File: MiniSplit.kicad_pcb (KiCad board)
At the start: 2 copper layers, 135 x 80 mm, 49 parts, among them J1 5PIN, SW1 SW_PUSH, SW10 SW_PUSH, SW11 SW_PUSH, SW12 SW_PUSH, SW13 SW_PUSH, SW14 SW_PUSH, SW15 SW_PUSH, SW16 SW_PUSH, SW17 SW_PUSH, SW18 SW_PUSH, SW19 SW_PUSH, SW2 SW_PUSH, SW20 SW_PUSH, SW21 SW_PUSH, SW3 SW_PUSH, SW4 SW_PUSH, SW5 SW_PUSH, SW6 SW_PUSH, SW7 SW_PUSH, SW8 SW_PUSH, SW9 SW_PUSH, U1 HOLE, U1 ProMicro, U2 HOLE, U3 HOLE, U4 HOLE

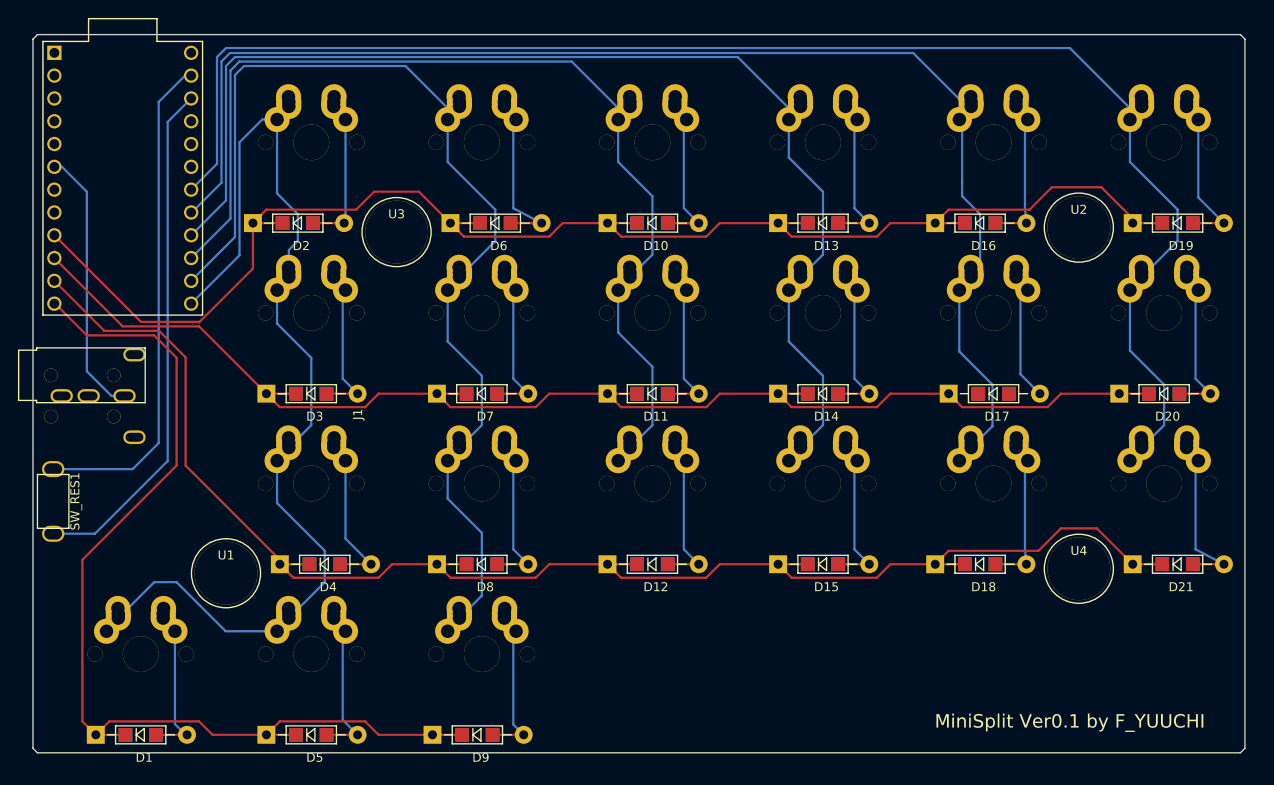
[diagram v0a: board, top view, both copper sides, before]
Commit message: ✨ver0.1→0.2✨
fix:Switch Hole,TRRS Jack Silk
add:icon
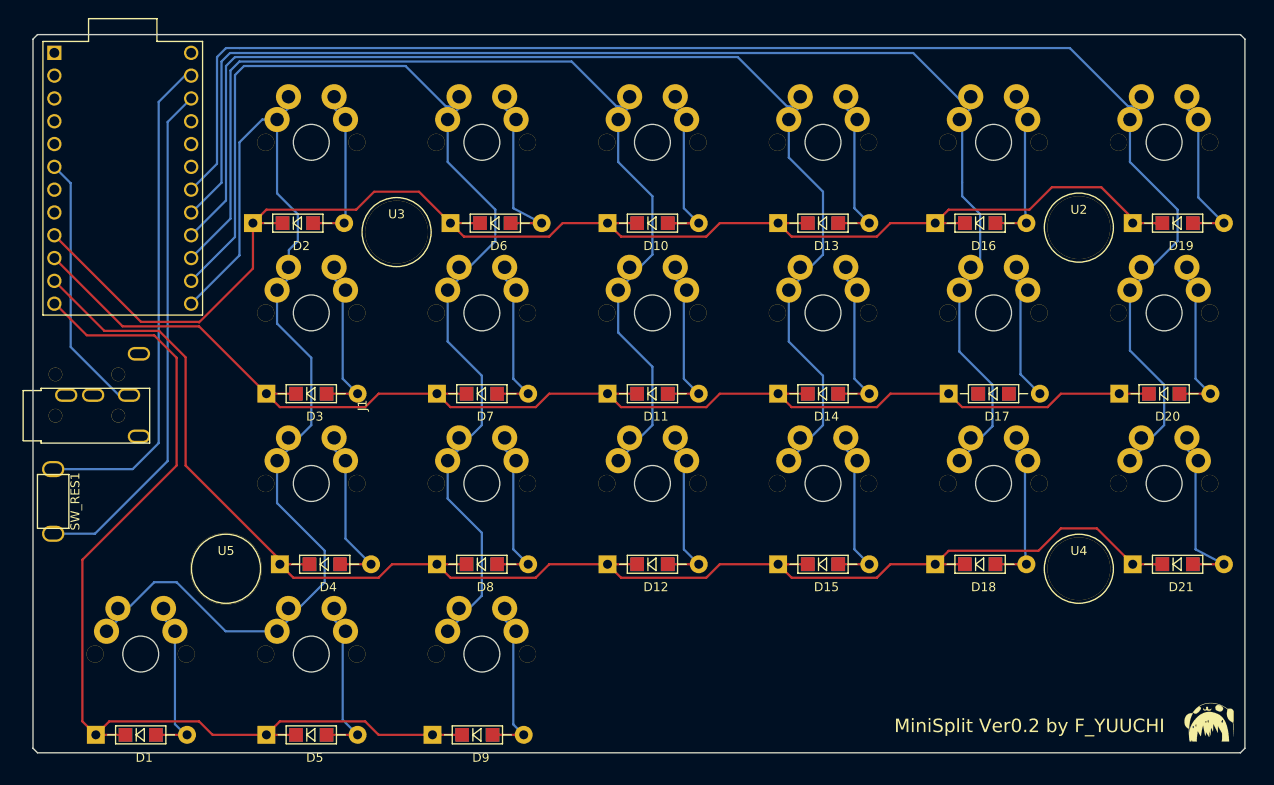
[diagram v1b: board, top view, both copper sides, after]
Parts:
- removed the U1 at (121.5, 110.0)
- added G***: LOGO, minisplit-footprint:icon_logo, F.Cu at (231.0, 126.0)
- added U5: HOLE, library:hole, F.Cu at (121.5, 109.5)
- SW1, SW10, SW11, SW12, SW13, SW14, SW15, SW16, SW17, SW18, SW19, SW2, SW20, SW21, SW3, SW4, SW5, SW6, SW7, SW8, SW9: footprint lets_split-footprint:MXALPS_FLIP_HOLES -> minisplit-footprint:MX_FLIP_HOLES
- moved J1 1.12 mm to (113.0, 90.0)
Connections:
- J1 pad 1: VCC -> (no net)
- J1 pad 2: Net-(J1-Pad2) -> (no net)
- U1 pad 1: Net-(U1-Pad1) -> (no net)
- U1 pad 19: Net-(U1-Pad19) -> (no net)
- U1 pad 2: Net-(U1-Pad2) -> (no net)
- U1 pad 20: Net-(U1-Pad20) -> (no net)
- U1 pad 21: Net-(U1-Pad21) -> (no net)
- U1 pad 24: Net-(U1-Pad24) -> (no net)
- U1 pad 3: Net-(U1-Pad3) -> (no net)
- U1 pad 4: Net-(U1-Pad4) -> (no net)
- U1 pad 5: Net-(U1-Pad5) -> (no net)
- U1 pad 7: Net-(U1-Pad7) -> (no net)
- U1 pad 8: Net-(U1-Pad8) -> (no net)
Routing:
- net col4: track 147.3 -> 151.3 mm
- net sda: track 30.1 -> 29.5 mm
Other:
- board text added: "MiniSplit Ver0.2 by F_YUUCHI"
- board text removed: "MiniSplit Ver0.1 by F_YUUCHI"

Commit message: SizeCange
130mm×85mm→127mm×83.5mm
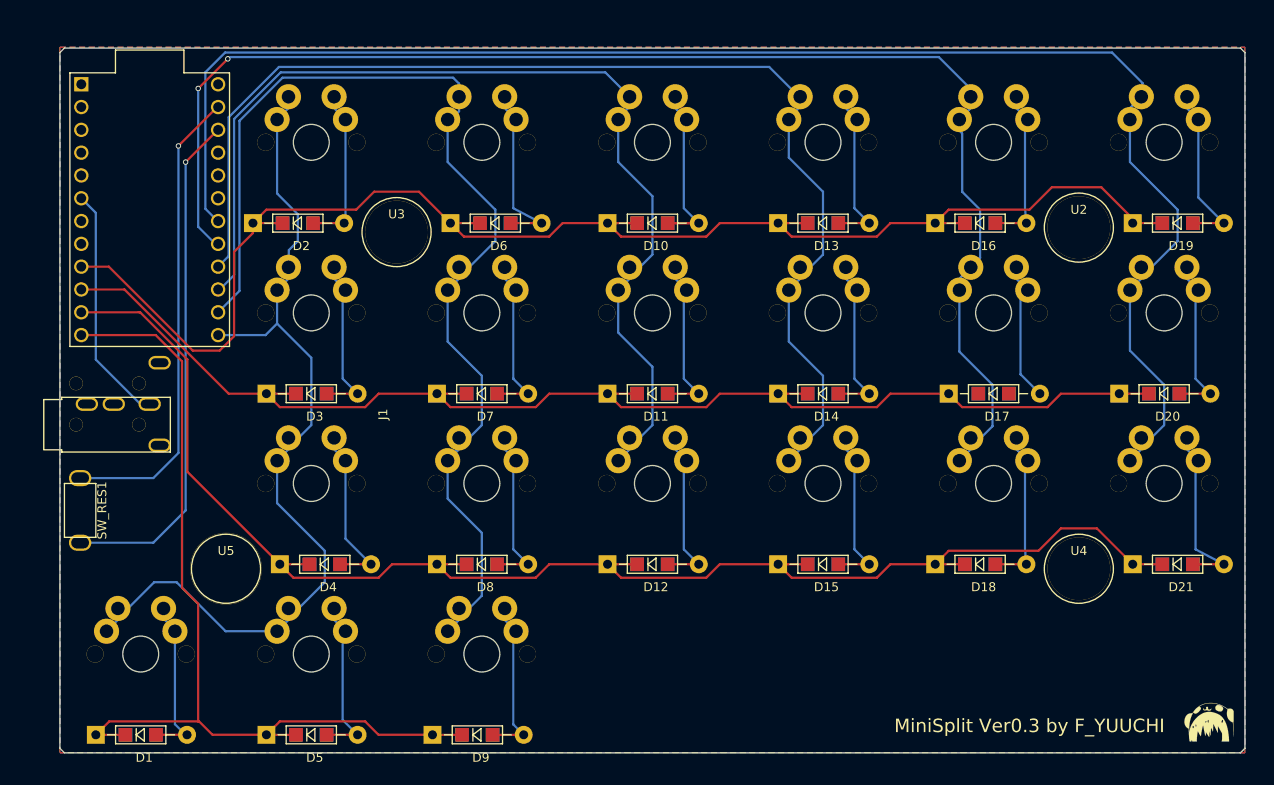
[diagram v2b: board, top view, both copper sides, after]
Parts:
- moved U1 4.61 mm to (113.0, 69.5)
- moved SW_RES1 3.16 mm to (107.0, 103.0)
- moved J1 2.51 mm to (115.3, 91.0)
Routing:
- net col0: track 117.5 -> 99.2 mm
- net row3: track 113.0 -> 103.2 mm
- net col4: track 151.3 -> 156.2 mm, vias 0 -> 2
- net row1: track 147.6 -> 143.2 mm
- net col5: track 169.8 -> 174.1 mm
- net row2: track 168.6 -> 164.7 mm
- net GND: track 55.8 -> 52.5 mm, vias 0 -> 1
- net sda: track 29.5 -> 26.7 mm
- net col2: track 116.0 -> 113.5 mm
- net col3: track 133.5 -> 132.1 mm
- net row0: track 162.2 -> 163.6 mm
- net Net-(SW_RES1-Pad1): track 57.6 -> 57.1 mm, vias 0 -> 1
- added copper zone on B.Cu, net GND
- added copper zone on F.Cu, net GND
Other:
- board size 135 x 80 mm -> 132 x 78.5 mm
- board text added: "MiniSplit Ver0.3 by F_YUUCHI"
- board text removed: "MiniSplit Ver0.2 by F_YUUCHI"

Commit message: ✨ver0.2→1.0✨
42keys→50keys
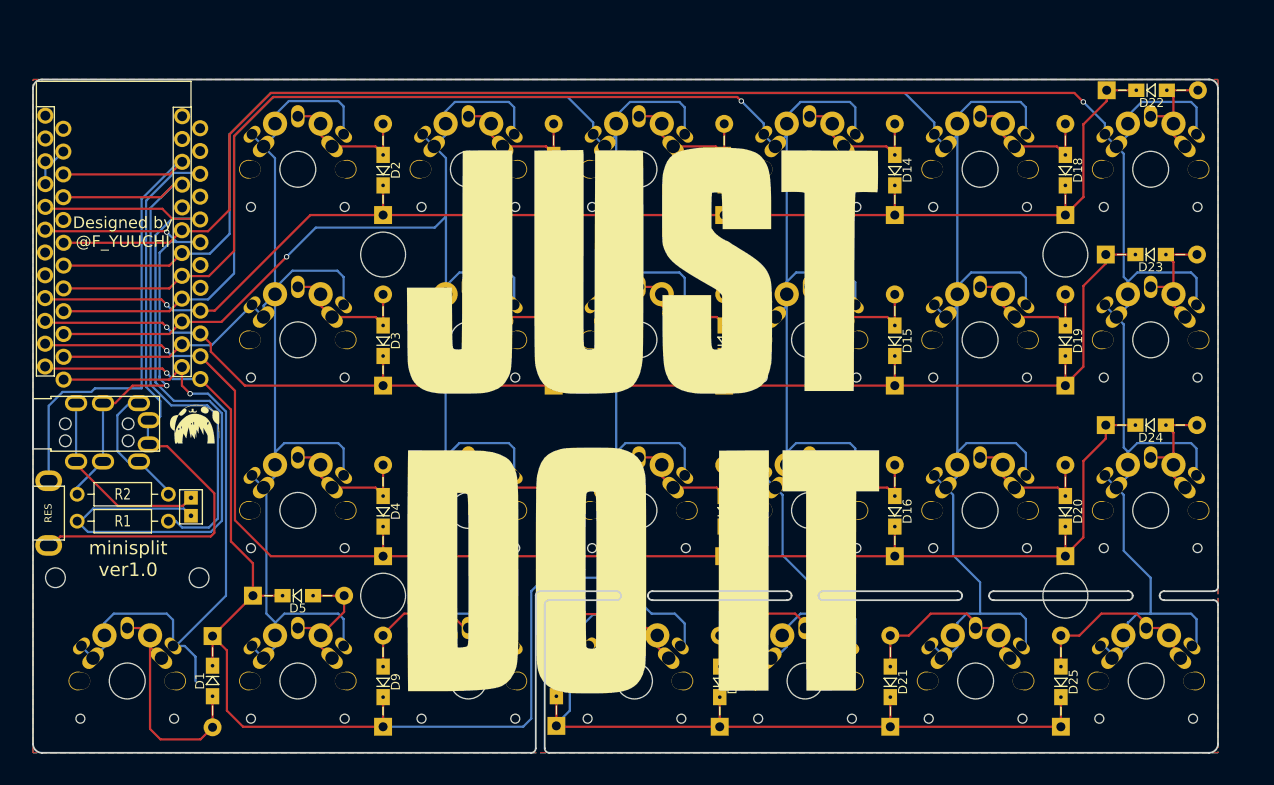
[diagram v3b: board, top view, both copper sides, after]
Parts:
- removed the G*** at (231.0, 126.0)
- removed SW1, SW10, SW11, SW12, SW13, SW14, SW15, SW16, SW17, SW18, SW19, SW2, SW20, SW21, SW3, SW4, SW5, SW6, SW7, SW8, SW9: SW_PUSH, minisplit-footprint:MX_FLIP_HOLES
- removed SW_RES1: SW_PUSH, minisplit-footprint:TACT_SWITCH_TVBP06
- removed the U1 at (113.0, 69.5)
- removed U2, U3, U4, U5: HOLE, library:hole
- added D22: D, minisplit2-footprint:Diode_TH_SOD123, F.Cu at (224.6, 56.2)
- added D23: D, minisplit2-footprint:Diode_TH_SOD123, F.Cu at (224.5, 74.5)
- added D24: D, minisplit2-footprint:Diode_TH_SOD123, F.Cu at (224.5, 93.5)
- added D25: D, minisplit2-footprint:Diode_TH_SOD123, F.Cu at (214.5, 122.1)
- added G***: LOGO, minisplit2-footprint:JUST_DO_IT, F.Cu at (168.0, 93.0)
- added G***: LOGO, minisplit2-footprint:icon_logo, F.Cu at (118.0, 92.8)
- added R1: R1, promicro:RESISTOR, F.Cu at (110.0, 104.2)
- added R2: R2, promicro:RESISTOR, F.Cu at (110.0, 101.2)
- added REF**: M2_HOLE, minisplit2-footprint:M2_HOLE, F.Cu at (102.5, 110.5)
- added REF**: M2_HOLE, minisplit2-footprint:M2_HOLE, F.Cu at (118.5, 110.5)
- added RES1: SW_PUSH, minisplit-footprint:TACT_SWITCH_TVBP06, F.Cu at (100.0, 103.3)
- added SW_1: SW_PUSH, minisplit2-footprint:MX_PG1350_FLIP_HOLES, F.Cu at (129.5, 65.0)
- added SW_11: SW_PUSH, minisplit2-footprint:MX_PG1350_FLIP_HOLES, F.Cu at (129.5, 84.0)
- added SW_12: SW_PUSH, minisplit2-footprint:MX_PG1350_FLIP_HOLES, F.Cu at (148.5, 84.0)
- added SW_13: SW_PUSH, minisplit2-footprint:MX_PG1350_FLIP_HOLES, F.Cu at (167.5, 84.0)
- added SW_14: SW_PUSH, minisplit2-footprint:MX_PG1350_FLIP_HOLES, F.Cu at (186.5, 84.0)
- added SW_15: SW_PUSH, minisplit2-footprint:MX_PG1350_FLIP_HOLES, F.Cu at (205.5, 84.0)
- added SW_16: SW_PUSH, minisplit2-footprint:MX_PG1350_FLIP_HOLES, F.Cu at (224.5, 84.0)
- added SW_2: SW_PUSH, minisplit2-footprint:MX_PG1350_FLIP_HOLES, F.Cu at (148.5, 65.0)
- added SW_21: SW_PUSH, minisplit2-footprint:MX_PG1350_FLIP_HOLES, F.Cu at (129.5, 103.0)
- added SW_22: SW_PUSH, minisplit2-footprint:MX_PG1350_FLIP_HOLES, F.Cu at (148.5, 103.0)
- added SW_23: SW_PUSH, minisplit2-footprint:MX_PG1350_FLIP_HOLES, F.Cu at (167.5, 103.0)
- added SW_24: SW_PUSH, minisplit2-footprint:MX_PG1350_FLIP_HOLES, F.Cu at (186.5, 103.0)
- added SW_25: SW_PUSH, minisplit2-footprint:MX_PG1350_FLIP_HOLES, F.Cu at (205.5, 103.0)
- added SW_26: SW_PUSH, minisplit2-footprint:MX_PG1350_FLIP_HOLES, F.Cu at (224.5, 103.0)
- added SW_3: SW_PUSH, minisplit2-footprint:MX_PG1350_FLIP_HOLES, F.Cu at (167.5, 65.0)
- added SW_30: SW_PUSH, minisplit2-footprint:MX_PG1350_FLIP_HOLES, F.Cu at (110.5, 122.0)
- added SW_31: SW_PUSH, minisplit2-footprint:MX_PG1350_FLIP_HOLES, F.Cu at (129.5, 122.0)
- added SW_32: SW_PUSH, minisplit2-footprint:MX_PG1350_FLIP_HOLES, F.Cu at (148.5, 122.0)
- added SW_33: SW_PUSH, minisplit2-footprint:MX_PG1350_FLIP_HOLES, F.Cu at (167.0, 122.0)
- added SW_34: SW_PUSH, minisplit2-footprint:MX_PG1350_FLIP_HOLES, F.Cu at (186.0, 122.0)
- added SW_35: SW_PUSH, minisplit2-footprint:MX_PG1350_FLIP_HOLES, F.Cu at (205.0, 122.0)
- added SW_36: SW_PUSH, minisplit2-footprint:MX_PG1350_FLIP_HOLES, F.Cu at (224.0, 122.0)
- added SW_4: SW_PUSH, minisplit2-footprint:MX_PG1350_FLIP_HOLES, F.Cu at (186.5, 65.0)
- added SW_5: SW_PUSH, minisplit2-footprint:MX_PG1350_FLIP_HOLES, F.Cu at (205.5, 65.0)
- added SW_6: SW_PUSH, minisplit2-footprint:MX_PG1350_FLIP_HOLES, F.Cu at (224.5, 65.0)
- added U1: ProMicro, minisplit2-footprint:ProMicro, B.Cu at (111.0, 74.4)
- added U1: ProMicro, minisplit2-footprint:ProMicro, F.Cu at (109.0, 73.0)
- added U_H1: HOLE, minisplit2-footprint:hole, F.Cu at (139.0, 74.5)
- added U_H2: HOLE, minisplit2-footprint:hole, F.Cu at (139.0, 112.5)
- added U_H3: HOLE, minisplit2-footprint:hole, F.Cu at (215.0, 74.5)
- added U_H4: HOLE, minisplit2-footprint:hole, F.Cu at (215.0, 112.5)
- added W1: jumper_smd, ergo42:jumper_smd_2dub, F.Cu at (117.6, 102.6)
- D1, D10, D11, D12, D13, D14, D15, D16, D17, D18, D19, D2, D20, D21, D3, D4, D5, D6, D7, D8, D9: footprint footprint:Diode_TH_SOD123 -> minisplit2-footprint:Diode_TH_SOD123
- moved D13 56.7 mm to (158.3, 122.0), turned to 90 degrees
- moved D18 46.2 mm to (215.0, 65.1), turned to 90 degrees
- moved D17 41.0 mm to (176.5, 122.1), turned to 90 degrees
- moved D16 32.4 mm to (196.0, 103.1), turned to 90 degrees
- moved D21 30.0 mm to (195.5, 122.1), turned to 90 degrees
- moved D14 28.1 mm to (196.0, 65.1), turned to 90 degrees
- moved D15 28.1 mm to (196.0, 84.1), turned to 90 degrees
- moved D5 15.9 mm to (129.5, 112.5)
- moved D2 15.7 mm to (139.0, 65.1), turned to 90 degrees
- moved D19 15.1 mm to (215.0, 84.1), turned to 90 degrees
- moved D20 14.4 mm to (215.0, 103.1), turned to 90 degrees
- moved D1 14.3 mm to (120.0, 122.0), turned to 270 degrees
- moved D10 14.3 mm to (177.0, 65.1), turned to 90 degrees
- moved D11 14.3 mm to (177.0, 84.1), turned to 90 degrees
- moved D12 14.3 mm to (177.0, 103.1), turned to 90 degrees
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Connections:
- D13 pad 1: row0 -> row3
- D14 pad 1: row1 -> row0
- D15 pad 1: row2 -> row1
- D16 pad 1: row0 -> row2
- D17 pad 1: row1 -> row3
- D18 pad 1: row2 -> row0
- D19 pad 1: row0 -> row1
- D20 pad 1: row1 -> row2
- D21 pad 1: row2 -> row3
- J1 pad 1: (no net) -> VCC
- J1 pad 2: (no net) -> /xtradata
- J1 pad 3: sda -> /sda/uart
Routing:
- net col6: track 0.00 -> 247.8 mm, vias 0 -> 1
- net row3: track 103.2 -> 221.3 mm, vias 0 -> 1
- net /scl: track 0.00 -> 91.8 mm
- net VCC: track 0.00 -> 82.4 mm
- net col3: track 132.1 -> 204.3 mm
- net col5: track 174.1 -> 239.0 mm
- net col4: track 156.2 -> 220.1 mm, vias 2 -> 1
- net /RES: track 0.00 -> 60.7 mm
- net col2: track 113.5 -> 173.1 mm, vias 0 -> 1
- net Net-(SW_RES1-Pad1): track 57.1 -> 0.00 mm, vias 1 -> 0
- net /sda/uart: track 0.00 -> 54.7 mm, vias 0 -> 2
- net sda: track 26.7 -> 0.00 mm
- net col0: track 99.2 -> 74.0 mm, vias 0 -> 1
- net GND: track 52.5 -> 74.5 mm, vias 1 -> 0
- net /xtradata: track 0.00 -> 21.9 mm
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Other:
- board size 132 x 78.5 mm -> 132 x 75 mm
- net class 1 added: clearance 0.2, trace_width 0.5, via_dia 0.6, via_drill 0.4
- net class 2 added: clearance 0.1, trace_width 0.25, via_dia 0.6, via_drill 0.4
- rule pad_to_mask_clearance: 0.2 -> 0.05
- board text added: "Designed by @F_YUUCHI"
- board text added: "minisplit ver1.0"
- board text removed: "MiniSplit Ver0.3 by F_YUUCHI"

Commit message: size fixed
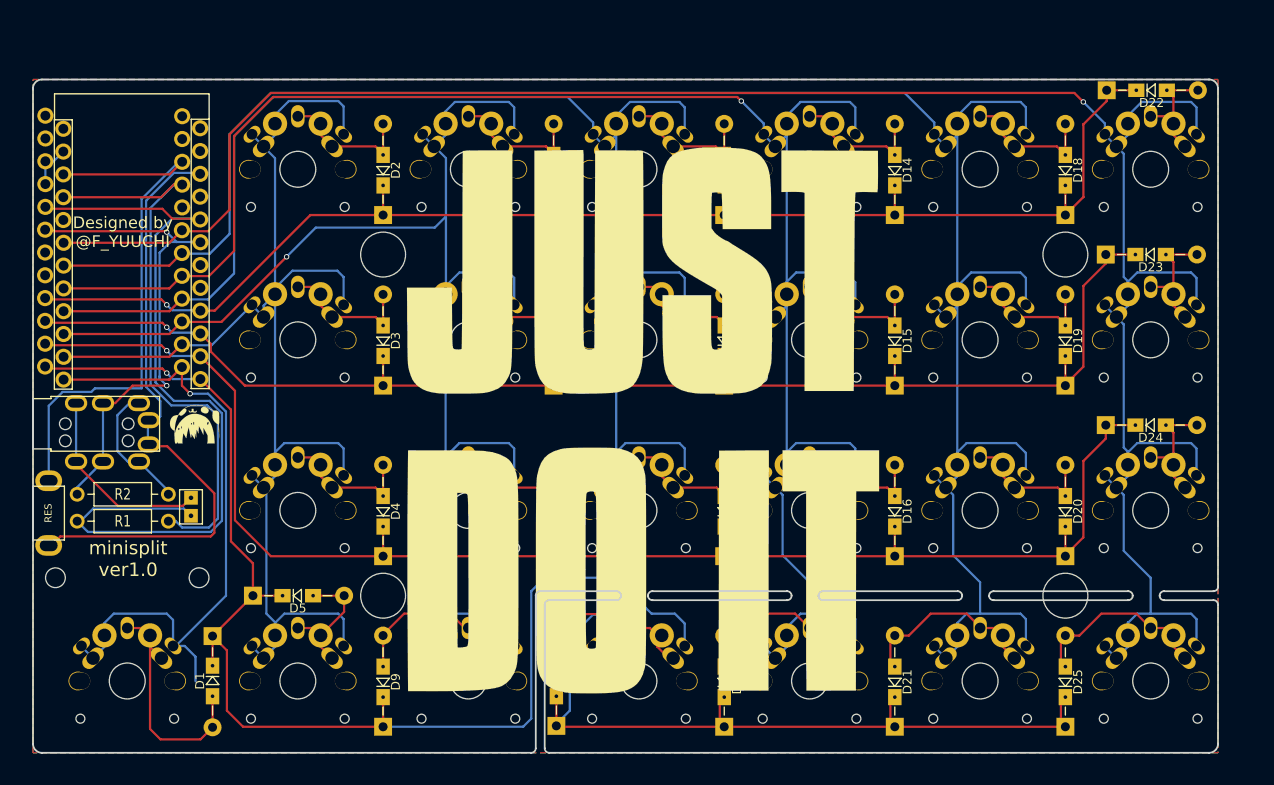
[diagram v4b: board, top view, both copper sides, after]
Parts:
- U1 (x2): footprint minisplit2-footprint:ProMicro -> minisplit-footprint:ProMicro
- moved D17 0.50 mm to (177.0, 122.1)
- moved D21 0.50 mm to (196.0, 122.1)
- moved D25 0.50 mm to (215.0, 122.1)
- moved SW_33 0.50 mm to (167.5, 122.0)
- moved SW_34 0.50 mm to (186.5, 122.0)
- moved SW_35 0.50 mm to (205.5, 122.0)
- moved SW_36 0.50 mm to (224.5, 122.0)
